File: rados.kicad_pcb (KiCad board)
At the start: 2 copper layers, 83.2 x 106 mm, 155 parts, among them J1 HEADER, J10 STEPSTICK, J11 STEPSTICK, J12 STEPSTICK, J13 MICROSD_SLOT_TFP09-2-12B, J2 HEADER, J3 HEADER, J4 STEPSTICK, J5 STEPSTICK, J6 STEPSTICK, J7 HEADER, J8 HEADER, J9 HEADER, P1 CONN_01X02, P10 CONN_01X04, P11 CONN_01X04, P12 CONN_01X04, P13 EXT_SD, P14 LCD, P15 LIMIT_SWITCHES, P16 LIMIT_SWITCHES_V, P17 CONN_01X03, P18 CONN_01X03, P19 CONN_01X03, P2 CONN_01X02, P20 CONN_01X03, P21 THERMISTORS, P22 CONN_01X05, P3 CONN_01X02, P4 CONN_01X02, P5 HP_MOSFETS, P6 MP_MOSFETS, P7 CONN_02X04, P8 CONN_01X04, P9 CONN_01X04, Q1 2N7002P, Q10 2N7002P, Q11 2N7002P, Q12 BC846BPDW1, Q13 BC846BPDW1, Q14 SI2318CDS-T1-GE3, Q15 IRFB7545PbF, Q16 2N7002P, Q17 2N7002P, Q18 BC846BPDW1, Q19 BC846BPDW1, Q2 2N7002P, Q20 SI2318CDS-T1-GE3, Q21 IRFB7545PbF, Q3 2N7002P, Q4 BC846BPDW1, Q5 BC846BPDW1, Q6 BC846BPDW1, Q7 IRFB7545PbF, Q8 SI2318CDS-T1-GE3, Q9 IRFB7545PbF, SW1 RESET, U1 MC34063, U2 24LC256

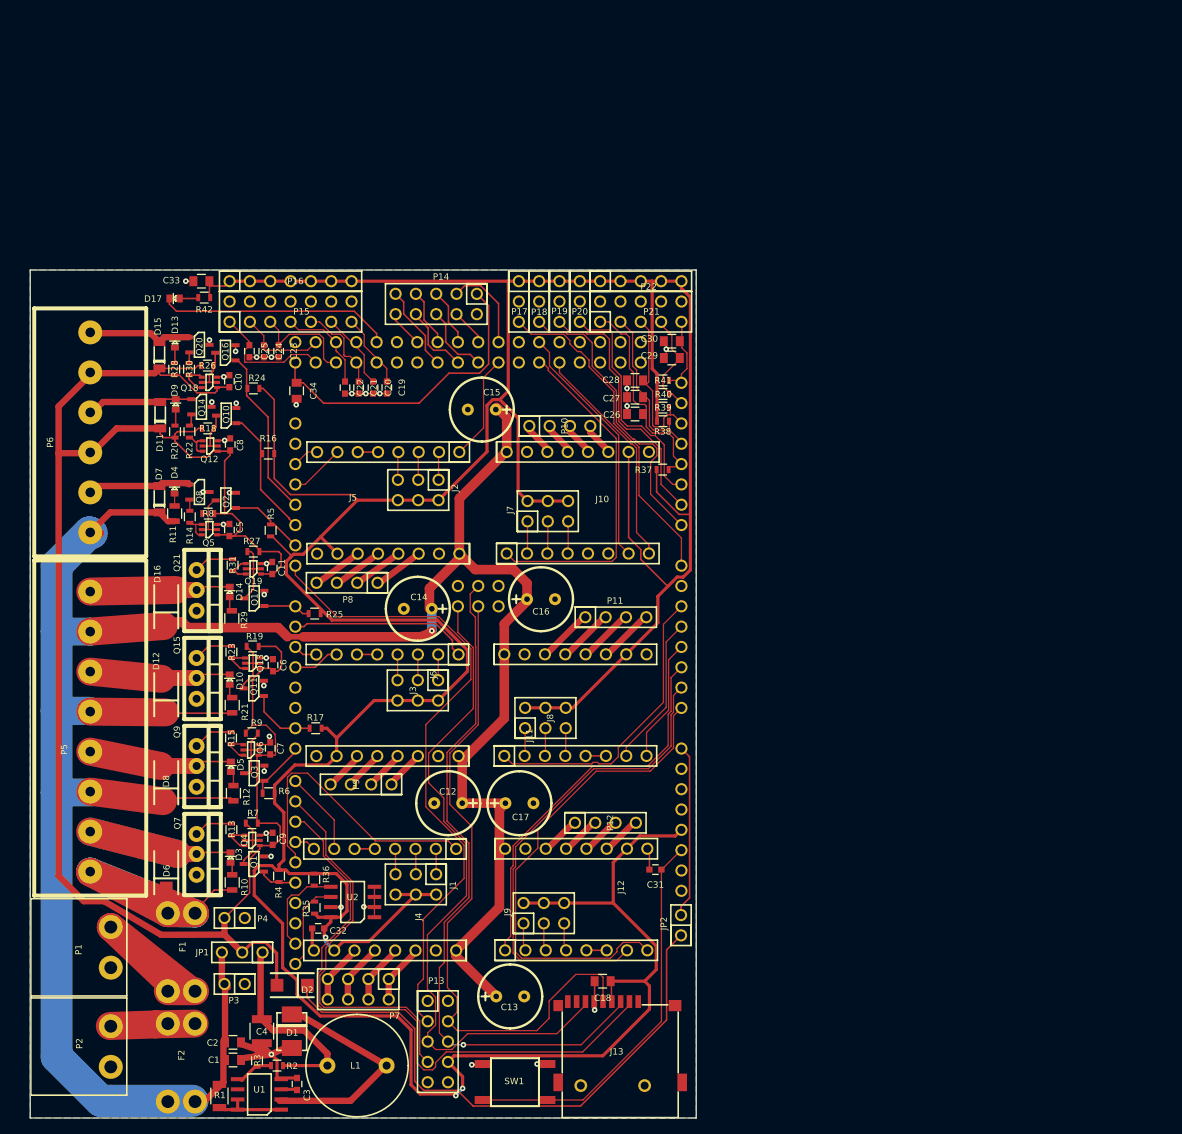
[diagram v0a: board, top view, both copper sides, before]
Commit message: - added wifi esp8266 - switched caps to smd - fixed dual transistor pinout bug
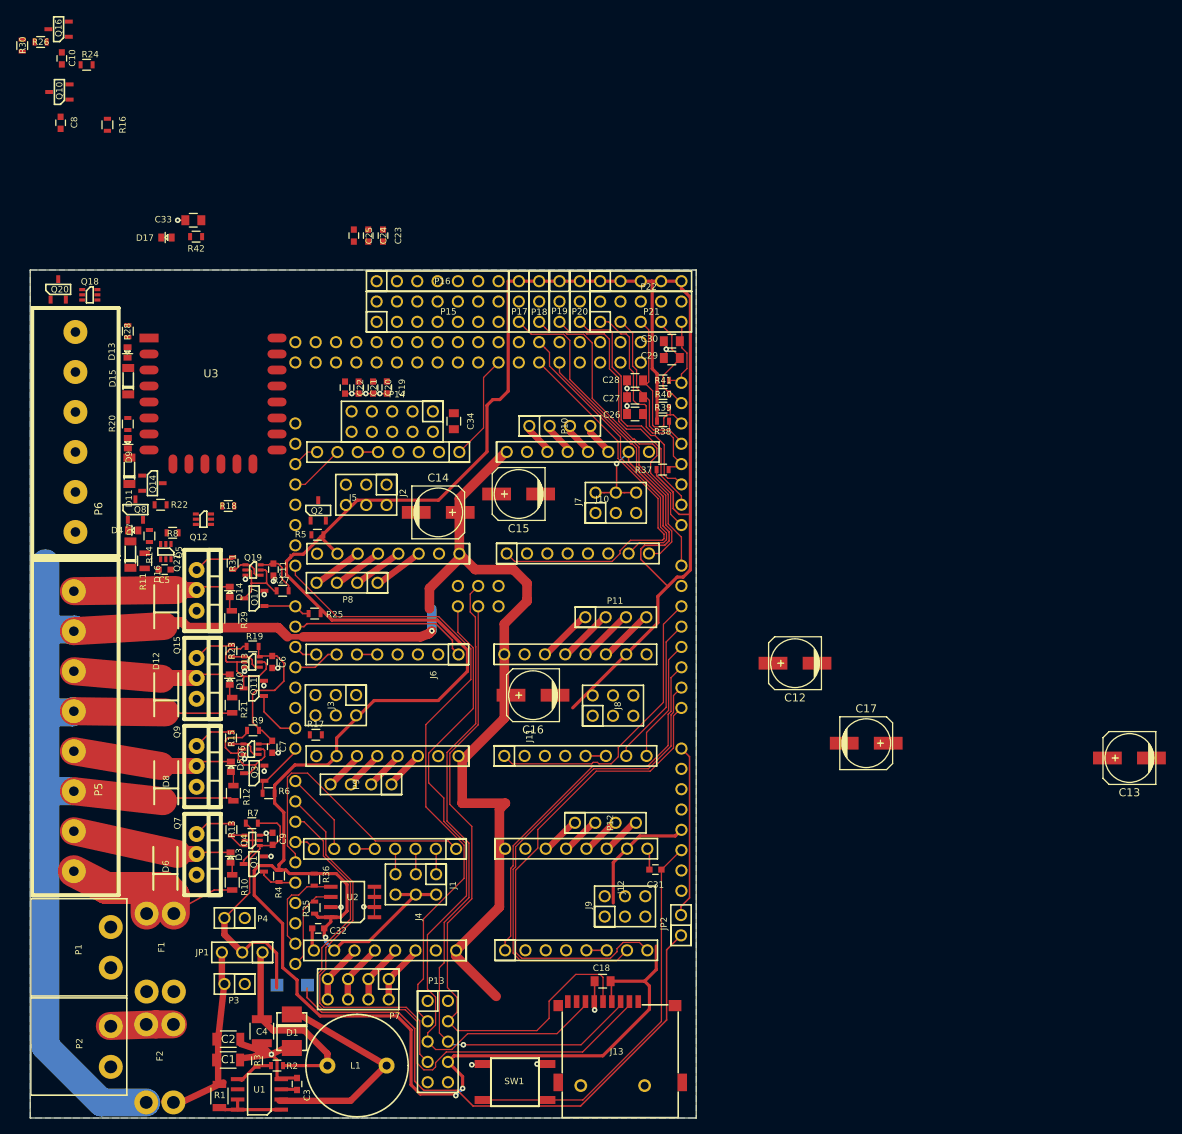
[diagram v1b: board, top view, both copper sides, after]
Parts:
- added U3: ESP-12E, misc:ESP-12E, F.Cu at (85.8, 32.5)
- C1, C2: footprint capacitors:C_0805 -> capacitors:C_1206
- C12, C13, C14, C15, C16, C17: footprint capacitors:ELCO-8mm-3.5mm_pitch -> capacitors:c_elec_6.3x7.7
- D2: moved to B.Cu
- moved C13 84.7 mm to (208.4, 85.0), turned to 180 degrees
- moved R16 45.8 mm to (80.7, 5.85), turned to 270 degrees
- moved C17 45.5 mm to (175.5, 83.2)
- moved Q10 45.5 mm to (74.7, 1.75)
- moved Q16 45.5 mm to (74.5, -6.10)
- moved R24 45.5 mm to (78.0, -1.65)
- moved R26 45.5 mm to (72.3, -4.50)
- moved R30 45.5 mm to (70.0, -4.05)
- moved C10 45.5 mm to (75.0, -2.45), turned to 270 degrees
- moved C8 45.4 mm to (74.8, 5.60), turned to 270 degrees
- moved C12 45.0 mm to (166.6, 73.2)
- moved C34 20.0 mm to (124.0, 42.9)
- moved C23 19.5 mm to (115.1, 19.7)
- moved C24 19.5 mm to (113.2, 19.7)
- moved C25 19.5 mm to (111.5, 19.7)
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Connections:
- Q12 pad 1: +12V -> Net-(Q12-Pad1)
- Q12 pad 4: Net-(Q12-Pad4) -> Net-(Q12-Pad1)
- Q12 pad 6: Net-(Q12-Pad4) -> +12V
- Q13 pad 1: +12V -> Net-(Q13-Pad1)
- Q13 pad 4: Net-(Q13-Pad4) -> Net-(Q13-Pad1)
- Q13 pad 6: Net-(Q13-Pad4) -> +12V
- Q18 pad 1: +12V -> Net-(Q18-Pad1)
- Q18 pad 4: Net-(Q18-Pad4) -> Net-(Q18-Pad1)
- Q18 pad 6: Net-(Q18-Pad4) -> +12V
- Q19 pad 1: +12V -> Net-(Q19-Pad1)
- Q19 pad 4: Net-(Q19-Pad4) -> Net-(Q19-Pad1)
- Q19 pad 6: Net-(Q19-Pad4) -> +12V
- Q4 pad 1: +12V -> Net-(Q4-Pad1)
- Q4 pad 4: Net-(Q4-Pad4) -> Net-(Q4-Pad1)
- Q4 pad 6: Net-(Q4-Pad4) -> +12V
- Q5 pad 1: +12V -> Net-(Q5-Pad1)
- Q5 pad 4: Net-(Q5-Pad4) -> Net-(Q5-Pad1)
- Q5 pad 6: Net-(Q5-Pad4) -> +12V
- Q6 pad 1: +12V -> Net-(Q6-Pad1)
- Q6 pad 4: Net-(Q6-Pad4) -> Net-(Q6-Pad1)
- Q6 pad 6: Net-(Q6-Pad4) -> +12V
- R13 pad 1: Net-(Q4-Pad4) -> Net-(Q4-Pad1)
- R14 pad 1: Net-(Q5-Pad4) -> Net-(Q5-Pad1)
- R15 pad 1: Net-(Q6-Pad4) -> Net-(Q6-Pad1)
- R22 pad 1: Net-(Q12-Pad4) -> Net-(Q12-Pad1)
- R23 pad 1: Net-(Q13-Pad4) -> Net-(Q13-Pad1)
- R30 pad 1: Net-(Q18-Pad4) -> Net-(Q18-Pad1)
- R31 pad 1: Net-(Q19-Pad4) -> Net-(Q19-Pad1)
- SHIELD1 pad 16: LP-FET1 -> ESP-RX
- SHIELD1 pad 17: LP-FET2 -> ESP-TX
- SHIELD1 pad 20: SDA -> LP-FET1
- SHIELD1 pad 21: SCL -> LP-FET2
- SHIELD1 pad 28: PROBE -> Probe
- U1 pad 6: Net-(U1-Pad6) -> Vsupply
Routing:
- net +12V: track 238.0 -> 58.9 mm
- net +3V3: track 528.5 -> 430.2 mm, vias 3 -> 4
- net +5V: track 38.7 -> 0.00 mm
- net Vheatbed: track 63.1 -> 31.4 mm
- net STATUS-LED: track 29.2 -> 0.00 mm
- net Net-(F1-Pad1): track 27.9 -> 0.00 mm
- net Vsupply: track 322.1 -> 298.5 mm
- net LP-FET2: track 21.3 -> 0.00 mm
- net X-: track 16.0 -> 0.00 mm
- net LP-FET1: track 16.2 -> 0.24 mm
- net GND: track 77.7 -> 62.4 mm, vias 33 -> 24
- net Y-: track 14.1 -> 0.00 mm
- net LP-OUT1: track 13.6 -> 0.00 mm
- net MP-OUT1: track 13.4 -> 0.00 mm
- net LP-OUT2: track 12.9 -> 0.00 mm
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
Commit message: Routing
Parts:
- added P23: CONN_01X02, headers:CON_HDR_1x2_2.54mm, F.Cu at (95.5, 114.6)
- added P24: CONN_01X02, headers:CON_HDR_1x2_2.54mm, F.Cu at (95.5, 104.6)
- D2: moved to F.Cu
- moved C13 76.3 mm to (133.9, 101.4)
- moved C17 58.6 mm to (120.8, 104.2)
- moved C10 56.6 mm to (91.2, 51.8)
- moved Q10 55.6 mm to (95.2, 53.5)
- moved Q16 54.2 mm to (105.1, 38.7)
- moved R16 52.5 mm to (98.9, 55.0)
- moved R24 50.8 mm to (105.2, 41.2), turned to 180 degrees
- moved C12 42.9 mm to (124.2, 79.7), turned to 0 degrees
- moved R30 31.8 mm to (76.0, 27.1)
- moved R26 30.4 mm to (78.5, 25.2), turned to 0 degrees
- moved D17 23.0 mm to (109.3, 28.6), turned to 270 degrees
- moved C8 22.3 mm to (81.2, 26.9)
- moved C33 22.3 mm to (111.9, 26.4), turned to 270 degrees
- moved C25 20.6 mm to (120.8, 38.1)
- moved C24 20.5 mm to (122.3, 38.1)
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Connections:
- SHIELD1 pad 22: X- -> Net-(SHIELD1-Pad22)
- SHIELD1 pad 23: X+ -> Net-(SHIELD1-Pad23)
- SHIELD1 pad 24: Y- -> Net-(SHIELD1-Pad24)
- SHIELD1 pad 25: Y+ -> STATUS-LED
- SHIELD1 pad 26: Z- -> Net-(SHIELD1-Pad26)
- SHIELD1 pad 27: Z+ -> ENC-A
- SHIELD1 pad 28: Probe -> ENC-B
- SHIELD1 pad 29: STATUS-LED -> LCD-D5
- SHIELD1 pad 30: Net-(SHIELD1-Pad30) -> LCD-RS
- SHIELD1 pad 31: Net-(SHIELD1-Pad31) -> LCD-D6
- SHIELD1 pad 32: Net-(SHIELD1-Pad32) -> LCD-E
- SHIELD1 pad 33: LCD-D4 -> LCD-D7
- SHIELD1 pad 34: LCD-D7 -> LCD-D4
- SHIELD1 pad 35: LCD-D6 -> X-
- SHIELD1 pad 36: LCD-E -> X+
- SHIELD1 pad 37: LCD-D5 -> Y-
- SHIELD1 pad 38: LCD-RS -> Y+
- SHIELD1 pad 39: ENC-B -> Z-
- SHIELD1 pad 40: X-EN -> Z+
- SHIELD1 pad 41: ENC-A -> PROBE
- SHIELD1 pad 42: Net-(SHIELD1-Pad42) -> X-EN
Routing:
- net +12V: track 58.9 -> 218.9 mm
- net +3V3: track 430.2 -> 476.1 mm, vias 4 -> 3
- net Net-(F1-Pad1): track 0.00 -> 42.9 mm
- net Net-(Q16-Pad3): track 0.00 -> 37.7 mm
- net ESP-RX: track 0.00 -> 25.9 mm
- net Vheatbed: track 31.4 -> 55.8 mm
- net ESP-TX: track 0.00 -> 24.0 mm
- net SCL1: track 11.3 -> 34.5 mm
- net SDA1: track 12.0 -> 31.0 mm
- net Vsupply: track 298.5 -> 317.3 mm, vias 1 -> 2
- net MP-OUT1: track 0.00 -> 17.3 mm
- net X-: track 0.00 -> 14.8 mm
- net LP-OUT2: track 0.00 -> 14.0 mm
- net X+: track 0.00 -> 13.5 mm
- net LP-OUT1: track 0.00 -> 12.7 mm
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
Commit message: Lots of routing
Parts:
- moved Q2 8.08 mm to (99.7, 57.4), turned to 180 degrees
- moved Q10 5.00 mm to (100.2, 53.2)
- moved R5 4.67 mm to (102.2, 57.5), turned to 90 degrees
- moved R16 4.52 mm to (100.0, 50.6), turned to 180 degrees
- moved R24 0.40 mm to (105.6, 41.4), turned to 0 degrees
- moved C9 0.31 mm to (97.0, 95.2), turned to 270 degrees
- moved D17 0.14 mm to (109.2, 28.5)
- turned Q4 to 0 degrees
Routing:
- net +3V3: track 476.1 -> 582.1 mm, vias 3 -> 4
- net +12V: track 218.9 -> 283.0 mm
- net GND: track 51.9 -> 95.9 mm, vias 19 -> 47
- net Vsupply: track 317.3 -> 337.8 mm
- net Net-(Q2-Pad3): track 0.00 -> 13.2 mm
- net RESET: track 48.9 -> 61.4 mm
- net Net-(J3-Pad1): track 0.00 -> 12.4 mm
- net Net-(J3-Pad5): track 0.00 -> 12.4 mm
- net Net-(J3-Pad3): track 0.00 -> 12.4 mm
- net LP-FET1: track 0.24 -> 12.3 mm
- net Net-(J12-Pad3): track 0.40 -> 12.3 mm
- net Net-(J12-Pad4): track 0.27 -> 12.1 mm
- net Net-(J12-Pad2): track 0.55 -> 12.4 mm
- net Net-(J10-Pad4): track 0.11 -> 10.8 mm
- net Net-(J10-Pad3): track 0.13 -> 10.8 mm
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
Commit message: some refinements
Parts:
- R42: value 4K7 -> 470R
- turned C12 to 180 degrees
- turned C13 to 0 degrees
- turned C14 to 180 degrees
- turned C15 to 0 degrees
- turned C16 to 0 degrees
- turned C17 to 180 degrees
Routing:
- net +12V: track 283.0 -> 284.0 mm
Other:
- board size 83.2 x 106 mm -> 83.5 x 106 mm
- board text added: "+"
- board text added: "-"
- board text added: "12V"
- board text added: "24V"
- board text added: "E1"
- board text added: "E2"
- board text added: "E3"
- board text added: "S1"
- board text added: "S2"
- board text added: "S3"
- board text added: "X"
- board text added: "Y"
- board text added: "Z"

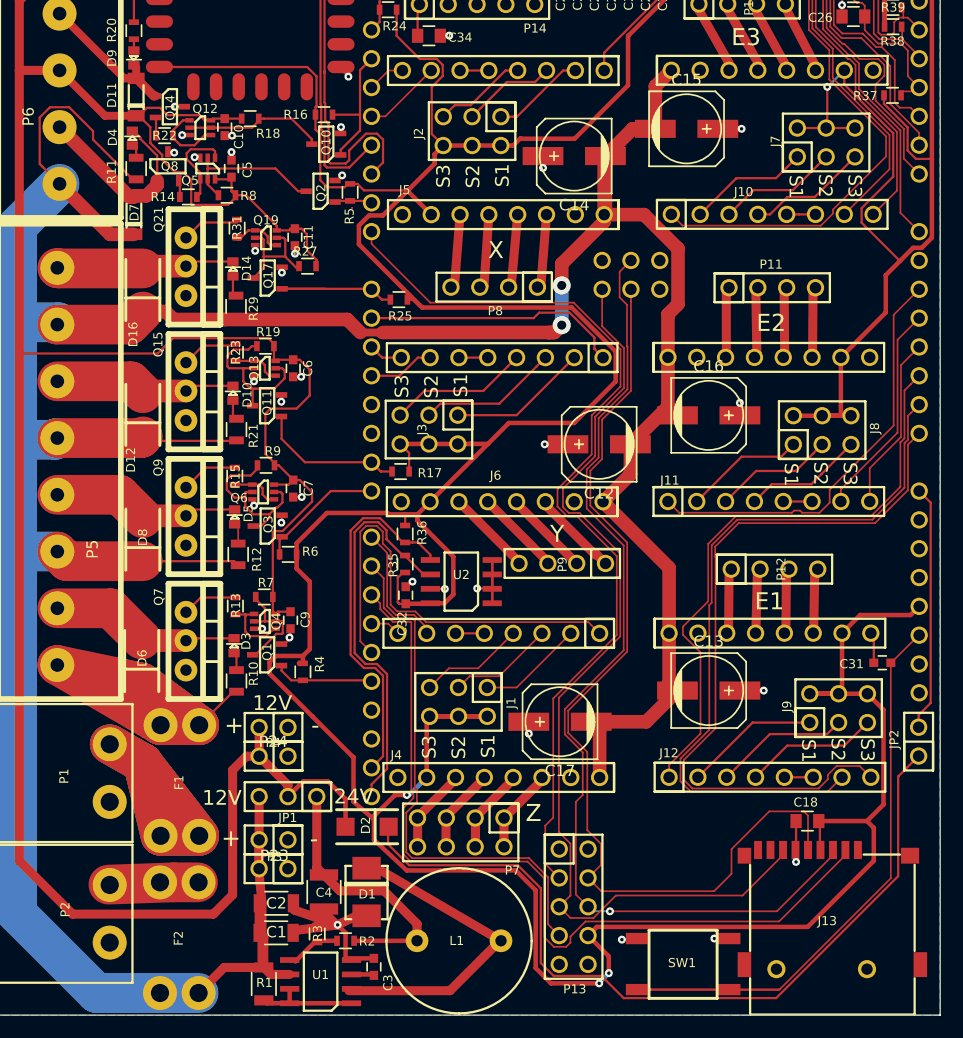
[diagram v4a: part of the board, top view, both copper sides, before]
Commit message: Replaced SMPS with ST ic
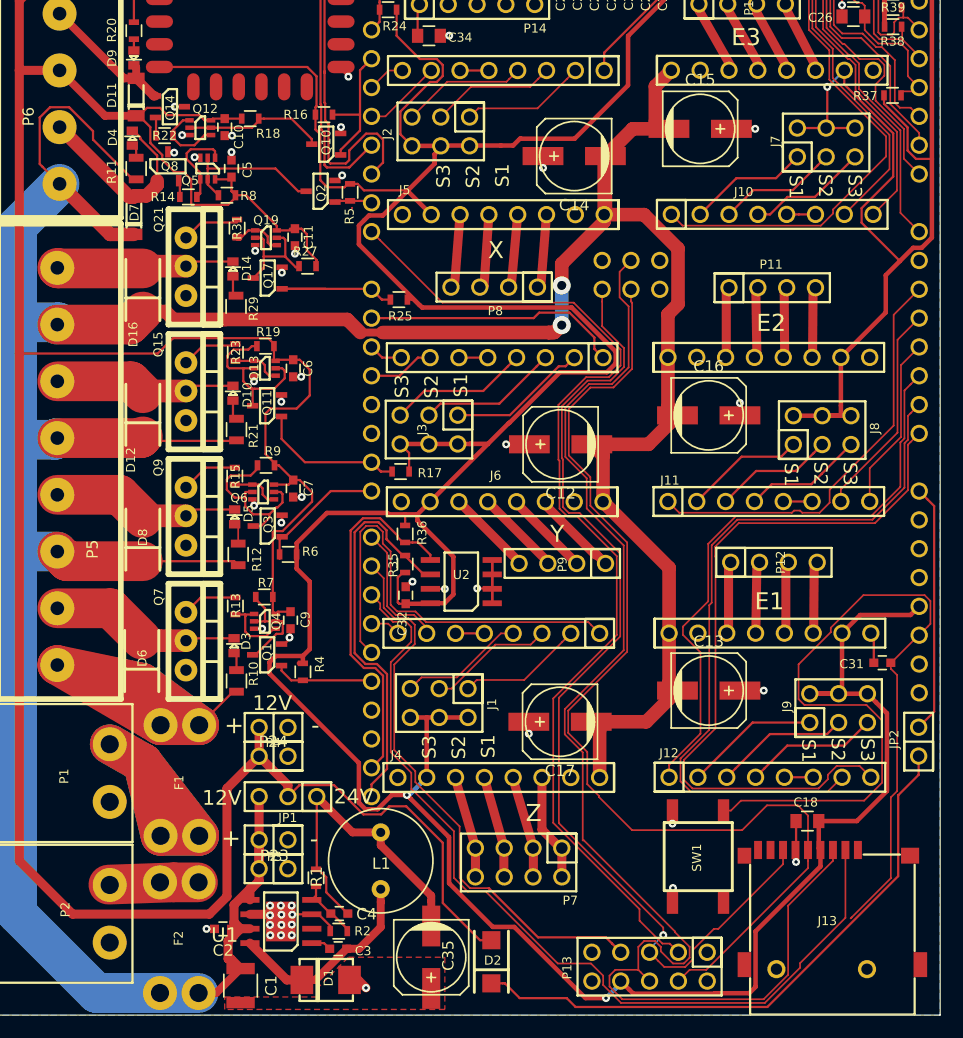
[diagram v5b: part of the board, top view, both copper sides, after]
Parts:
- removed R3: 1K1, resistors:R_0603
- added C35: 33uF, capacitors:c_elec_6.3x7.7, F.Cu at (109.4, 124.9)
- C1: value 10uF -> 4.7uF; footprint capacitors:C_1206 -> capacitors:C_1210
- C2: value 10uF -> 100nF; footprint capacitors:C_1206 -> capacitors:C_0603
- C3: value 220pF -> 100nF
- C4: value 47uF -> DNP; footprint capacitors:C_1210 -> capacitors:C_0603
- D1: value STPS3L40UF -> STPS2L40UF
- L1: value 100uH -> 18uF; footprint inductors:INDUCTOR_AIUR06 -> inductors:INDUCTOR_BOURNS_RLB914
- R1: value 0.22R -> 620K; footprint resistors:R_1206 -> resistors:R_0603
- R2: value 10K -> 68K
- U1: value MC34063 -> ST1S14PHR; footprint soic:SOIC8 -> soic:HSOP8
- moved D2 16.5 mm to (114.7, 127.2), turned to 270 degrees
- moved SW1 13.2 mm to (134.9, 114.4), turned to 270 degrees
- moved L1 10.9 mm to (105.0, 118.9), turned to 90 degrees
- moved R1 10.4 mm to (99.2, 117.9)
- moved D1 8.79 mm to (99.7, 126.2), turned to 180 degrees
- moved P13 8.52 mm to (128.6, 125.7), turned to 270 degrees
- moved U1 6.35 mm to (96.2, 121.8)
- moved P7 5.75 mm to (117.1, 116.5)
- moved C1 5.61 mm to (92.6, 127.4), turned to 270 degrees
- moved C2 5.22 mm to (91.0, 122.4), turned to 180 degrees
- moved C3 3.53 mm to (101.2, 124.2), turned to 180 degrees
- moved C12 3.40 mm to (120.8, 79.7)
- moved J2 2.76 mm to (110.2, 52.1)
- moved C4 2.33 mm to (101.3, 121.0), turned to 180 degrees
- moved J1 1.70 mm to (110.1, 102.5)
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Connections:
- C3 pad 2: GND -> Net-(C3-Pad2)
- C4 pad 1: Net-(C4-Pad1) -> Net-(C35-Pad1)
- C4 pad 2: GND -> Net-(C4-Pad2)
- D1 pad 1: Net-(D1-Pad1) -> Net-(C3-Pad1)
- JP1 pad 1: Net-(C4-Pad1) -> Net-(C35-Pad1)
- L1 pad 1: Net-(D1-Pad1) -> Net-(C3-Pad1)
- L1 pad 2: Net-(C4-Pad1) -> Net-(C35-Pad1)
- R1 pad 1: Vsupply -> Net-(C35-Pad1)
- R1 pad 2: Net-(R1-Pad2) -> Net-(C4-Pad2)
- R2 pad 1: Net-(C4-Pad1) -> Net-(C4-Pad2)
- R2 pad 2: Net-(R2-Pad2) -> GND
- U1 pad 1: Net-(R1-Pad2) -> Net-(C3-Pad2)
- U1 pad 2: Net-(D1-Pad1) -> Net-(U1-Pad2)
- U1 pad 3: Net-(C3-Pad1) -> GND
- U1 pad 4: GND -> Net-(C4-Pad2)
- U1 pad 5: Net-(R2-Pad2) -> Vsupply
- U1 pad 6: Vsupply -> GND
- U1 pad 7: Net-(R1-Pad2) -> Vsupply
- U1 pad 8: Net-(R1-Pad2) -> Net-(C3-Pad1)
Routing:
- net SD-MOSI: track 88.3 -> 117.4 mm, vias 1 -> 0
- net Net-(C35-Pad1): track 0.00 -> 29.0 mm
- net Net-(D1-Pad1): track 28.6 -> 0.00 mm
- net Net-(C4-Pad1): track 24.3 -> 0.00 mm
- net Net-(D2-Pad1): track 71.4 -> 52.8 mm
- net +12V: track 284.0 -> 302.1 mm
- net RESET: track 61.4 -> 77.6 mm
- net Net-(C3-Pad1): track 2.28 -> 18.4 mm
- net +3V3: track 582.1 -> 566.1 mm, vias 4 -> 3
- net SD2-CS: track 81.5 -> 92.7 mm
- net Net-(R1-Pad2): track 9.13 -> 0.00 mm
- net SD-SCK: track 85.7 -> 94.8 mm
- net Net-(C4-Pad2): track 0.00 -> 5.73 mm
- net Net-(R2-Pad2): track 4.93 -> 0.00 mm
- net SD-MISO: track 86.0 -> 90.1 mm, vias 0 -> 1
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- added copper zone on F.Cu, net GND
